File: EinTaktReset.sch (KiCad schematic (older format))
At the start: 57 parts, among them IC1 74LS624, P1 CONN_02X10, P2 CONN_01X01, P3 CONN_01X01, P4 CONN_02X10, P8 CONN_01X01, P9 CONN_01X01, SW1 SPST, SW10 SPST, SW11 SPST, SW12 SPST, SW13 SPST, SW2 SWITCH_INV, SW3 SPST, SW4 SPST, SW5 SPST, SW6 SWITCH_INV, SW7 SPST, SW8 SPST, SW9 SPST, U1 74LS132, U2 74540En, U3 74HCT541_PWR, U4 74LS32, U5 74LS00, U6 74LS132

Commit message: Schrauben Klemmen wegen library arbeit wieder entfernt
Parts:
- removed J? (x3): 691213710003, PCB Terminal Blocks:691213710003, symbol PCB~Terminal~Blocks:691213710003
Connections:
- wire segments 269 -> 241
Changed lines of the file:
@@
 EESchema Schematic File Version 4
-LIBS:EinTaktReset-cache
 EELAYER 26 0
 EELAYER END
@@
 	2050 7400 2050 7800
 Wire Wire Line
-	2050 7800 2150 7800
-Wire Wire Line
 	4850 7700 4850 7300
 Wire Wire Line
@@
 Wire Wire Line
 	4950 1750 4950 1600
-Wire Wire Line
-	2350 6900 2100 6900
 Wire Wire Line
 	2050 6900 2050 7200
@@
 	6000 12300 6000 12800
 Wire Wire Line
-	2350 1000 2350 1150
-Wire Wire Line
-	7300 1000 7300 1150
-Wire Wire Line
-	2350 2050 2350 2200
-Wire Wire Line
-	7300 2050 7300 2200
-Wire Wire Line
-	2350 1150 2350 1250
-Connection ~ 2350 1150
-Wire Wire Line
-	2350 1250 2350 1350
-Connection ~ 2350 1250
-Wire Wire Line
-	2350 1450 2350 1350
-Connection ~ 2350 1350
-Wire Wire Line
-	2350 1450 2350 1550
-Connection ~ 2350 1450
-Wire Wire Line
-	2350 1650 2350 1750
-Wire Wire Line
-	2350 1850 2350 1950
-Wire Wire Line
-	2350 2050 2350 1950
-Connection ~ 2350 2050
-Connection ~ 2350 1950
-Wire Wire Line
-	2350 1850 2350 1750
-Connection ~ 2350 1850
-Connection ~ 2350 1750
-Wire Wire Line
-	2350 1650 2350 1550
-Connection ~ 2350 1650
-Connection ~ 2350 1550
-Wire Wire Line
-	7300 1150 7300 1250
-Connection ~ 7300 1150
-Wire Wire Line
-	7300 1250 7300 1350
-Connection ~ 7300 1250
-Wire Wire Line
-	7300 1350 7300 1450
-Connection ~ 7300 1350
-Wire Wire Line
-	7300 1450 7300 1550
-Connection ~ 7300 1450
-Wire Wire Line
-	7300 1550 7300 1650
-Connection ~ 7300 1550
-Wire Wire Line
-	7300 1650 7300 1750
-Connection ~ 7300 1650
-Wire Wire Line
-	7300 1750 7300 1850
-Connection ~ 7300 1750
-Wire Wire Line
-	7300 1850 7300 1950
-Connection ~ 7300 1850
-Wire Wire Line
-	7300 1950 7300 2050
-Connection ~ 7300 1950
-Connection ~ 7300 2050
-Wire Wire Line
 	4250 3250 4250 3900
 Wire Wire Line
@@
 Wire Wire Line
 	4450 14900 4450 15000
-Connection ~ 2150 7800
-Wire Wire Line
-	2150 7800 2350 7800
-Connection ~ 2100 6900
-Wire Wire Line
-	2100 6900 2050 6900
-Connection ~ 2350 7800
 Wire Wire Line
 	3750 7300 3750 7700
@@
 Wire Wire Line
 	5400 8300 5400 8500
-Connection ~ 5400 8500
-Connection ~ 5750 8500
-Wire Wire Line
-	5750 8500 10650 8500
-Wire Wire Line
-	5400 8500 5750 8500
-Wire Wire Line
-	5950 6100 5750 6100
-Wire Wire Line
-	5650 6100 5750 6100
-Connection ~ 5750 6100
 Wire Wire Line
 	4850 7300 5650 7300
@@
 Wire Wire Line
 	3150 4650 3150 4950
-Wire Wire Line
-	5150 3150 5250 3150
-Connection ~ 5250 3150
-Wire Wire Line
-	5250 3150 5450 3150
-Connection ~ 5450 3150
-Wire Wire Line
-	5450 3150 5650 3150
-Wire Wire Line
-	6850 2450 6850 2550
-Connection ~ 6850 2550
-Wire Wire Line
-	6850 2550 6850 2650
-Connection ~ 2500 5950
-Wire Wire Line
-	2500 5950 3000 5950
-Wire Wire Line
-	2350 5950 2500 5950
 Wire Wire Line
 	1850 10650 1850 10600
@@
 	2600 2200 2350 2200
 Connection ~ 3100 1500
-Connection ~ 5650 3150
 Connection ~ 6550 1500
 Connection ~ 7000 2200
 Wire Wire Line
 	7000 2200 6650 2200
-Connection ~ 8050 2450
-Connection ~ 8050 2650
 $Comp
 L power:GND #PWR031
@@
 	1    0    0    -1
 $EndComp
-$Comp
-L PCB~Terminal~Blocks:691213710003 J?
-U 1 1 5A989AD2
-P 10550 3150
-F 0 "J?" H 10515 3190 50  0000 L CNN
-F 1 "691213710003" H 10515 3099 50  0000 L CNN
-F 2 "PCB Terminal Blocks:691213710003" H 10550 3150 50  0001 L BNN
-F 3 "1.12 USD" H 10550 3150 50  0001 L BNN
-F 4 "Warning" H 10550 3150 50  0001 L BNN "Field4"
-F 5 "Wurth Electronics" H 10550 3150 50  0001 L BNN "Field5"
-F 6 "TERM BLK 5MM HORZ ENTRY MOD 3P" H 10550 3150 50  0001 L BNN "Field6"
-F 7 "None" H 10550 3150 50  0001 L BNN "Field7"
-F 8 "691213710003" H 10550 3150 50  0001 L BNN "Field8"
-	1    10550 3150
-	1    0    0    -1
-$EndComp
-$Comp
-L PCB~Terminal~Blocks:691213710003 J?
-U 1 1 5A989D4B
-P 13050 9700
-F 0 "J?" H 13015 9740 50  0000 L CNN
-F 1 "691213710003" H 13015 9649 50  0000 L CNN
-F 2 "PCB Terminal Blocks:691213710003" H 13050 9700 50  0001 L BNN
-F 3 "1.12 USD" H 13050 9700 50  0001 L BNN
-F 4 "Warning" H 13050 9700 50  0001 L BNN "Field4"
-F 5 "Wurth Electronics" H 13050 9700 50  0001 L BNN "Field5"
-F 6 "TERM BLK 5MM HORZ ENTRY MOD 3P" H 13050 9700 50  0001 L BNN "Field6"
-F 7 "None" H 13050 9700 50  0001 L BNN "Field7"
-F 8 "691213710003" H 13050 9700 50  0001 L BNN "Field8"
-	1    13050 9700
-	1    0    0    -1
-$EndComp
-$Comp
-L PCB~Terminal~Blocks:691213710003 J?
-U 1 1 5A989E29
-P 12900 11950
-F 0 "J?" H 12865 11990 50  0000 L CNN
-F 1 "691213710003" H 12865 11899 50  0000 L CNN
-F 2 "PCB Terminal Blocks:691213710003" H 12900 11950 50  0001 L BNN
-F 3 "1.12 USD" H 12900 11950 50  0001 L BNN
-F 4 "Warning" H 12900 11950 50  0001 L BNN "Field4"
-F 5 "Wurth Electronics" H 12900 11950 50  0001 L BNN "Field5"
-F 6 "TERM BLK 5MM HORZ ENTRY MOD 3P" H 12900 11950 50  0001 L BNN "Field6"
-F 7 "None" H 12900 11950 50  0001 L BNN "Field7"
-F 8 "691213710003" H 12900 11950 50  0001 L BNN "Field8"
-	1    12900 11950
-	1    0    0    -1
-$EndComp
 Wire Wire Line
 	12700 11400 12700 11850
@@
 Wire Wire Line
 	4150 14900 4450 14900
+Wire Wire Line
+	2050 7800 2350 7800
+Wire Wire Line
+	2050 6900 2350 6900
+Wire Wire Line
+	5400 8500 10650 8500
+Wire Wire Line
+	5650 6100 5950 6100
+Wire Wire Line
+	5150 3150 5650 3150
+Wire Wire Line
+	6850 2450 6850 2650
+Wire Wire Line
+	2350 5950 3000 5950
 Wire Bus Line
 	3100 1350 3100 1500
@@
 Wire Bus Line
 	3100 1500 3100 2050
+Wire Wire Line
+	2350 1000 2350 2200
+Wire Wire Line
+	7300 1000 7300 2200
 Wire Bus Line
 	3100 1500 6550 1500

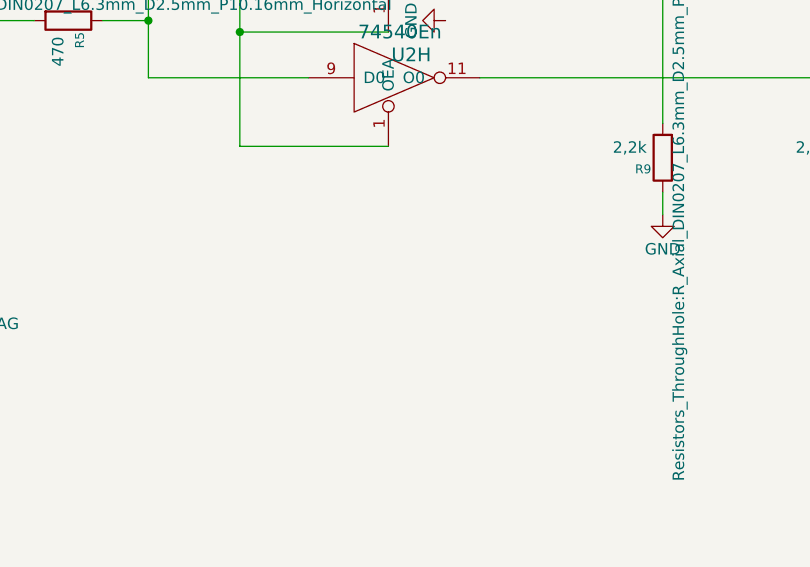
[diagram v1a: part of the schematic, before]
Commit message: Library Test put old Libs in bonsaicomplib
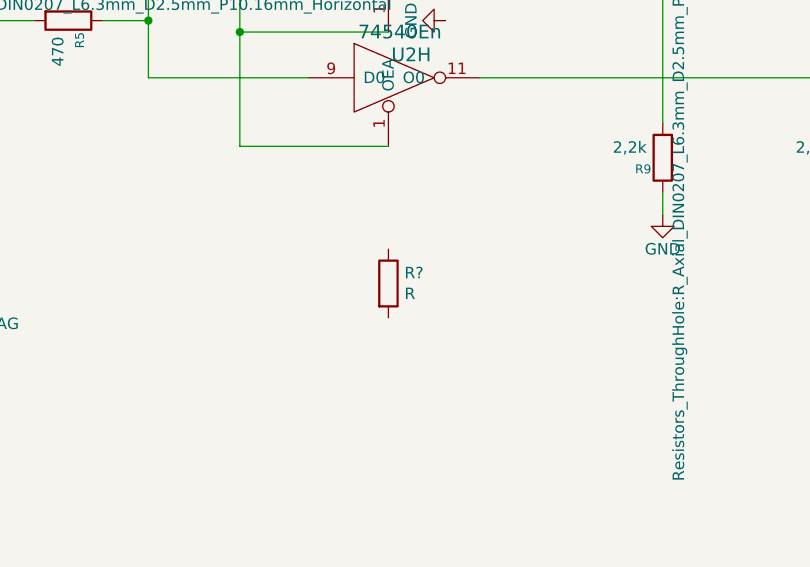
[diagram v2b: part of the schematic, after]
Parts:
- added R?: R, symbol bonsai:R
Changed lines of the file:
@@
 EESchema Schematic File Version 4
+LIBS:EinTaktReset-cache
 EELAYER 26 0
 EELAYER END
@@
 Wire Wire Line
 	2350 5950 3000 5950
+Wire Wire Line
+	2350 1000 2350 2200
+Wire Wire Line
+	7300 1000 7300 2200
 Wire Bus Line
 	3100 1350 3100 1500
@@
 Wire Bus Line
 	3100 1500 3100 2050
-Wire Wire Line
-	2350 1000 2350 2200
-Wire Wire Line
-	7300 1000 7300 2200
 Wire Bus Line
 	3100 1500 6550 1500
+$Comp
+L bonsai:R R?
+U 1 1 5ABE15F8
+P 6650 14400
+F 0 "R?" H 6720 14446 50  0000 L CNN
+F 1 "R" H 6720 14355 50  0000 L CNN
+F 2 "" V 6580 14400 30  0000 C CNN
+F 3 "" H 6650 14400 30  0000 C CNN
+	1    6650 14400
+	1    0    0    -1
+$EndComp
 $EndSCHEMATC

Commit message: TerminalBlochTested
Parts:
- added J1, J2: 3PinTerminalBlocktg, 3PinTerminalBlocktg, symbol 3PinTerminalBlocktg:3PinTerminalBlocktg
- gave numbers to parts that had none: 2
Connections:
- wire segments 241 -> 271
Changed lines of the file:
@@
 	3800 8400 3900 8400
-Wire Wire Line
-	5400 8300 5400 8500
 Wire Wire Line
 	4850 7300 5650 7300
@@
 	9050 3750 10350 3750
 $Comp
-L bonsai:D D?
+L bonsai:D D3
 U 1 1 5AA50448
 P 3850 15800
-F 0 "D?" H 3850 15585 50  0000 C CNN
+F 0 "D3" H 3850 15585 50  0000 C CNN
 F 1 "D" H 3850 15676 50  0000 C CNN
 F 2 "" H 3850 15800 60  0000 C CNN
@@
 	4150 14900 4450 14900
 Wire Wire Line
-	2050 7800 2350 7800
-Wire Wire Line
-	2050 6900 2350 6900
-Wire Wire Line
-	5400 8500 10650 8500
-Wire Wire Line
-	5650 6100 5950 6100
-Wire Wire Line
-	5150 3150 5650 3150
-Wire Wire Line
-	6850 2450 6850 2650
+	5400 8500 5750 8500
 Wire Wire Line
 	2350 5950 3000 5950
-Wire Wire Line
-	2350 1000 2350 2200
-Wire Wire Line
-	7300 1000 7300 2200
-Wire Bus Line
-	3100 1350 3100 1500
-Wire Bus Line
-	6550 1150 6550 1500
-Wire Bus Line
-	6550 1500 6550 1850
-Wire Bus Line
-	3100 1500 3100 2050
-Wire Bus Line
-	3100 1500 6550 1500
-$Comp
-L bonsai:R R?
+$Comp
+L bonsai:R R14
 U 1 1 5ABE15F8
 P 6650 14400
-F 0 "R?" H 6720 14446 50  0000 L CNN
+F 0 "R14" H 6720 14446 50  0000 L CNN
 F 1 "R" H 6720 14355 50  0000 L CNN
 F 2 "" V 6580 14400 30  0000 C CNN
@@
 	1    0    0    -1
 $EndComp
+$Comp
+L 3PinTerminalBlocktg:3PinTerminalBlocktg J2
+U 1 1 5ABEE025
+P 13050 9700
+F 0 "J2" H 13015 9740 50  0000 L CNN
+F 1 "3PinTerminalBlocktg" H 13015 9649 50  0000 L CNN
+F 2 "3PinTerminalBlocktg" H 13050 9700 50  0001 L BNN
+F 3 "1.12 USD" H 13050 9700 50  0001 L BNN
+F 4 "Warning" H 13050 9700 50  0001 L BNN "Field4"
+F 5 "Wurth Electronics" H 13050 9700 50  0001 L BNN "Field5"
+F 6 "TERM BLK 5MM HORZ ENTRY MOD 3P" H 13050 9700 50  0001 L BNN "Field6"
+F 7 "None" H 13050 9700 50  0001 L BNN "Field7"
+F 8 "3PinTerminalBlocktg" H 13050 9700 50  0001 L BNN "Field8"
+	1    13050 9700
+	1    0    0    -1
+$EndComp
+$Comp
+L 3PinTerminalBlocktg:3PinTerminalBlocktg J1
+U 1 1 5ABEE293
+P 12900 11950
+F 0 "J1" H 12865 11990 50  0000 L CNN
+F 1 "3PinTerminalBlocktg" H 12865 11899 50  0000 L CNN
+F 2 "3PinTerminalBlocktg" H 12900 11950 50  0001 L BNN
+F 3 "1.12 USD" H 12900 11950 50  0001 L BNN
+F 4 "Warning" H 12900 11950 50  0001 L BNN "Field4"
+F 5 "Wurth Electronics" H 12900 11950 50  0001 L BNN "Field5"
+F 6 "TERM BLK 5MM HORZ ENTRY MOD 3P" H 12900 11950 50  0001 L BNN "Field6"
+F 7 "None" H 12900 11950 50  0001 L BNN "Field7"
+F 8 "3PinTerminalBlocktg" H 12900 11950 50  0001 L BNN "Field8"
+	1    12900 11950
+	1    0    0    -1
+$EndComp
+Wire Wire Line
+	7300 1000 7300 1150
+Connection ~ 7300 1150
+Wire Wire Line
+	7300 1150 7300 1250
+Connection ~ 7300 1250
+Wire Wire Line
+	7300 1250 7300 1350
+Connection ~ 7300 1350
+Wire Wire Line
+	7300 1350 7300 1450
+Connection ~ 7300 1450
+Wire Wire Line
+	7300 1450 7300 1550
+Connection ~ 7300 1550
+Wire Wire Line
+	7300 1550 7300 1650
+Connection ~ 7300 1650
+Wire Wire Line
+	7300 1650 7300 1750
+Connection ~ 7300 1750
+Wire Wire Line
+	7300 1750 7300 1850
+Connection ~ 7300 1850
+Wire Wire Line
+	7300 1850 7300 1950
+Connection ~ 7300 1950
+Wire Wire Line
+	7300 1950 7300 2050
+Connection ~ 7300 2050
+Wire Wire Line
+	7300 2050 7300 2200
+Wire Wire Line
+	2350 1000 2350 1150
+Connection ~ 2350 2050
+Wire Wire Line
+	2350 2050 2350 2200
+Connection ~ 2350 1150
+Wire Wire Line
+	2350 1150 2350 1250
+Connection ~ 2350 1250
+Wire Wire Line
+	2350 1250 2350 1350
+Connection ~ 2350 1350
+Wire Wire Line
+	2350 1350 2350 1450
+Connection ~ 2350 1450
+Wire Wire Line
+	2350 1450 2350 1550
+Connection ~ 2350 1550
+Wire Wire Line
+	2350 1550 2350 1650
+Connection ~ 2350 1650
+Wire Wire Line
+	2350 1650 2350 1750
+Connection ~ 2350 1750
+Wire Wire Line
+	2350 1750 2350 1850
+Connection ~ 2350 1850
+Wire Wire Line
+	2350 1850 2350 1950
+Connection ~ 2350 1950
+Wire Wire Line
+	2350 1950 2350 2050
+Wire Wire Line
+	5150 3150 5250 3150
+Connection ~ 5250 3150
+Wire Wire Line
+	5250 3150 5450 3150
+Connection ~ 5450 3150
+Wire Wire Line
+	5450 3150 5650 3150
+Wire Wire Line
+	6850 2450 6850 2550
+Connection ~ 6850 2550
+Wire Wire Line
+	6850 2550 6850 2650
+Wire Wire Line
+	5650 6100 5750 6100
+Connection ~ 5750 6100
+Wire Wire Line
+	5750 6100 5950 6100
+Wire Wire Line
+	2050 6900 2100 6900
+Connection ~ 2100 6900
+Wire Wire Line
+	2100 6900 2350 6900
+Wire Wire Line
+	2050 7800 2150 7800
+Connection ~ 2150 7800
+Wire Wire Line
+	2150 7800 2350 7800
+Wire Wire Line
+	5400 8300 5400 8500
+Wire Wire Line
+	5400 8500 5750 8500
+Wire Bus Line
+	3100 1350 3100 1500
+Wire Bus Line
+	6550 1150 6550 1500
+Wire Bus Line
+	6550 1500 6550 1850
+Wire Bus Line
+	3100 1500 3100 2050
+Wire Bus Line
+	3100 1500 6550 1500
+Connection ~ 5400 8500
+Connection ~ 5800 8500
+Wire Wire Line
+	5800 8500 10650 8500
+Connection ~ 5750 8500
+Wire Wire Line
+	5750 8500 5800 8500
+Wire Wire Line
+	5750 8500 5800 8500
 $EndSCHEMATC
